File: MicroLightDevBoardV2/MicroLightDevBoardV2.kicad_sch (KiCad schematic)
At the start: 82 parts, among them J1 Conn_01x02_Socket, J10 Conn_01x02_Socket, J11 Conn_01x02_Socket, J12 TYPE-C-31-M-12, J13 Conn_01x02_Socket, J14 Conn_01x02_Socket, J15 Conn_01x02_Socket, J16 Conn_01x04_Socket, J17 Conn_01x02_Socket, J18 Conn_01x02_Socket, J19 Conn_01x04_Socket, J2 Conn_01x02_Socket, J20 Conn_01x04_Socket, J21 Conn_01x02_Socket, J22 Conn_01x02_Socket, J23 Conn_01x02_Socket, J24 Conn_01x02_Socket, J25 Conn_01x02_Socket, J26 Conn_01x04_Socket, J27 Conn_01x02_Socket, J28 Conn_01x04_Socket, J29 Conn_01x04_Socket, J3 Conn_01x04_Socket, J30 Conn_01x04_Socket, J31 Conn_01x04_Socket, J32 Conn_01x04_Socket, J33 Conn_01x04_Socket, J34 Conn_01x04_Socket, J35 Conn_01x04_Socket, J36 Conn_01x04_Socket, J37 Conn_01x04_Socket, J38 Conn_01x04_Socket, J39 Conn_01x04_Socket, J4 Conn_01x04_Socket, J40 Conn_01x04_Socket, J41 Conn_01x04_Socket, J42 Conn_01x04_Socket, J43 Conn_01x04_Socket, J44 Conn_01x04_Socket, J45 Conn_01x04_Socket, J46 Conn_01x04_Socket, J47 Conn_01x04_Socket, J48 Conn_01x04_Socket, J49 Conn_01x04_Socket, J5 Conn_01x05_Socket, J50 Conn_01x04_Socket, J6 Conn_01x05_Socket, J7 Conn_01x05_Socket, J8 Conn_01x05_Socket, J9 Conn_01x02_Socket, U1 BQ25180, U2 ATtiny3226-M, U3 S-85S1AB33-I6T1U, U4 B3U-1000P, U5 B3U-1000P, U6 USBLC6-2P6, U7 MC3479

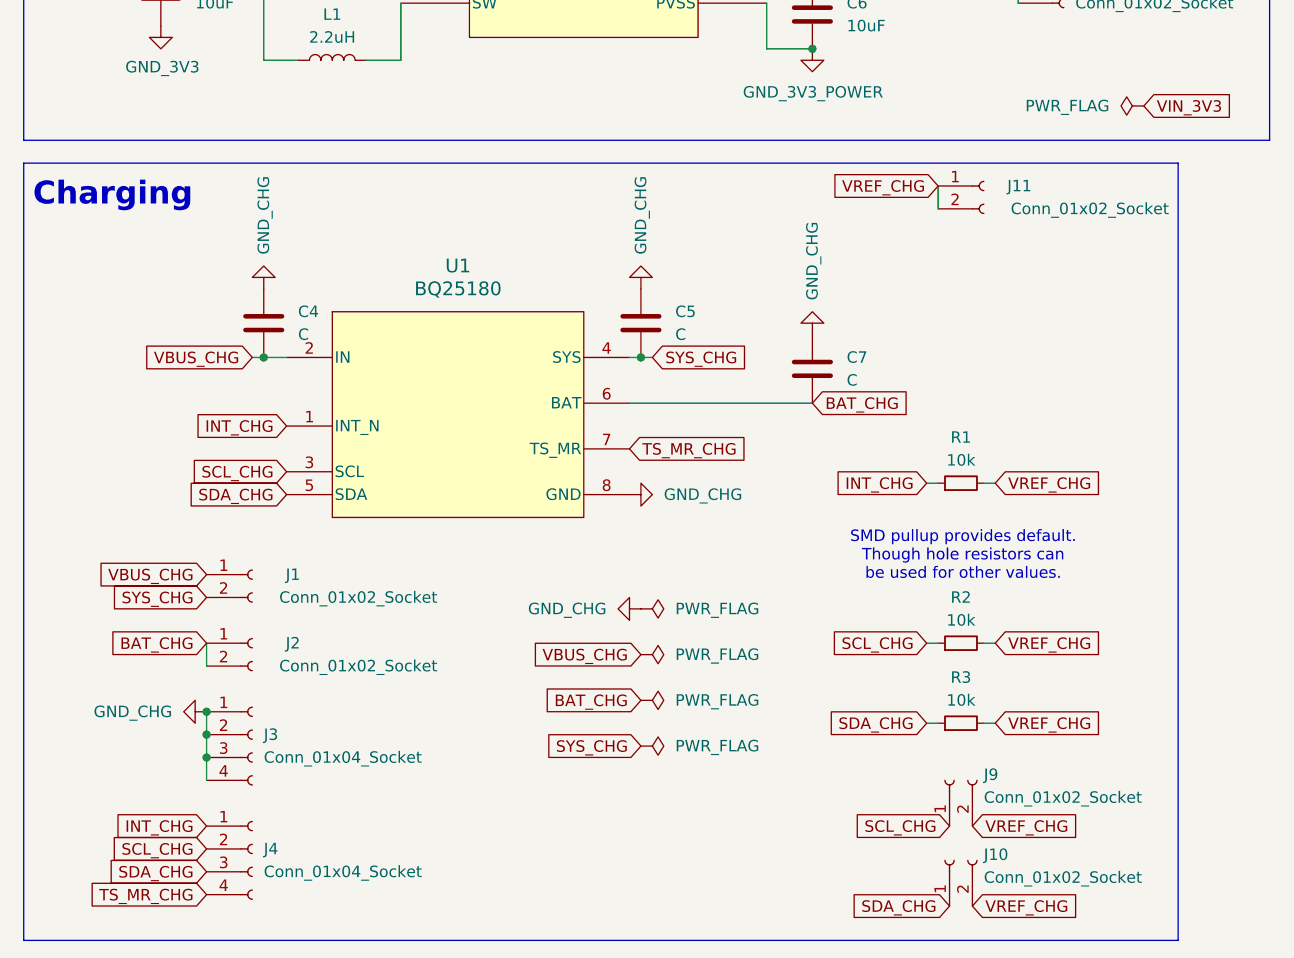
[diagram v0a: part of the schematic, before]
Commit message: added missing capacitorson charging ic pcb
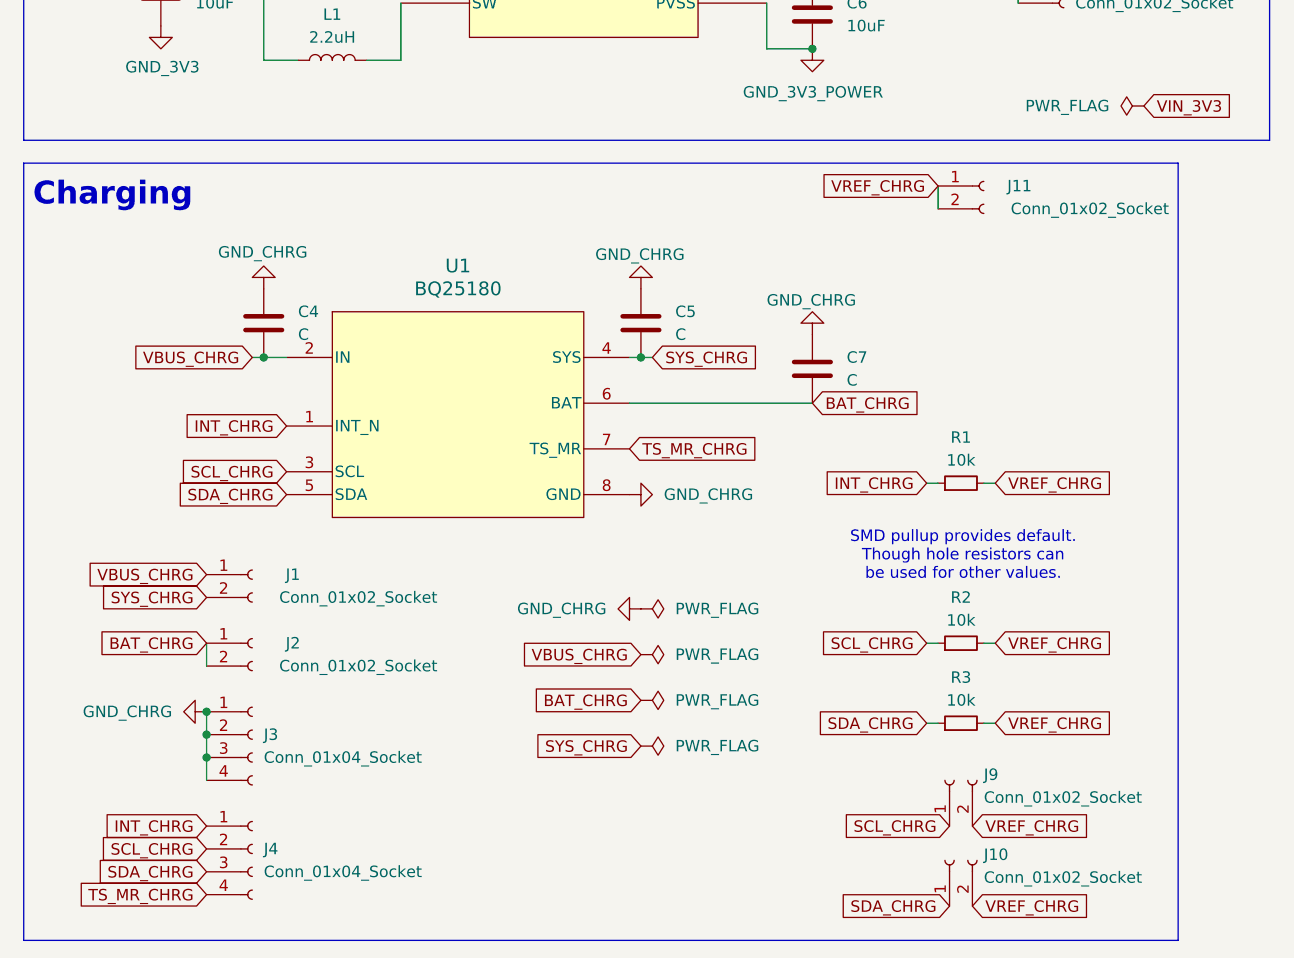
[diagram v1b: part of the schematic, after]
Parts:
- C4, C5, C7: footprint (none) -> Capacitor_SMD:C_0603_1608Metric
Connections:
- net BAT_CHG renamed BAT_CHRG
- net GND_CHG renamed GND_CHRG
- net INT_CHG renamed INT_CHRG
- net SCL_CHG renamed SCL_CHRG
- net SDA_CHG renamed SDA_CHRG
- net SYS_CHG renamed SYS_CHRG
- net TS_MR_CHG renamed TS_MR_CHRG
- net VBUS_CHG renamed VBUS_CHRG
- net VREF_CHG renamed VREF_CHRG
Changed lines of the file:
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@@
 		)
 	)
-	(global_label "VREF_CHG"
+	(global_label "VREF_CHRG"
 		(shape input)
 		(at 116.84 194.31 180)
@@
 		)
 		(property "Intersheetrefs" "${INTERSHEET_REFS}"
-			(at 104.4205 194.31 0)
+			(at 103.1505 194.31 0)
 			(effects
 				(font
@@
 		)
 	)
-	(global_label "TS_MR_CHG"
+	(global_label "TS_MR_CHRG"
 		(shape input)
 		(at 35.56 273.05 180)
@@
 		)
 		(property "Intersheetrefs" "${INTERSHEET_REFS}"
-			(at 21.8706 273.05 0)
+			(at 20.6006 273.05 0)
 			(effects
 				(font
@@
 		)
 	)
-	(global_label "BAT_CHG"
+	(global_label "BAT_CHRG"
 		(shape input)
 		(at 102.87 218.44 0)
@@
 		)
 		(property "Intersheetrefs" "${INTERSHEET_REFS}"
-			(at 114.0195 218.44 0)
+			(at 115.2895 218.44 0)
 			(effects
 				(font
@@
 		)
 	)
-	(global_label "VBUS_CHG"
+	(global_label "VBUS_CHRG"
 		(shape input)
 		(at 40.64 213.36 180)
@@
 		)
 		(property "Intersheetrefs" "${INTERSHEET_REFS}"
-			(at 27.9181 213.36 0)
+			(at 26.6481 213.36 0)
 			(effects
 				(font
@@
 		)
 	)
-	(global_label "BAT_CHG"
+	(global_label "BAT_CHRG"
 		(shape input)
 		(at 35.56 245.11 180)
@@
 		)
 		(property "Intersheetrefs" "${INTERSHEET_REFS}"
-			(at 24.4105 245.11 0)
+			(at 23.1405 245.11 0)
 			(effects
 				(font
@@
 		)
 	)
-	(global_label "VREF_CHG"
+	(global_label "VREF_CHRG"
 		(shape input)
 		(at 120.65 265.43 0)
@@
 		)
 		(property "Intersheetrefs" "${INTERSHEET_REFS}"
-			(at 133.0695 265.43 0)
+			(at 134.3395 265.43 0)
 			(effects
 				(font
@@
 		)
 	)
-	(global_label "SDA_CHG"
+	(global_label "SDA_CHRG"
 		(shape input)
 		(at 35.56 270.51 180)
@@
 		)
 		(property "Intersheetrefs" "${INTERSHEET_REFS}"
-			(at 24.1686 270.51 0)
+			(at 22.8986 270.51 0)
 			(effects
 				(font
@@
 		)
 	)
-	(global_label "SDA_CHG"
+	(global_label "SDA_CHRG"
 		(shape input)
 		(at 115.57 254 180)
@@
 		)
 		(property "Intersheetrefs" "${INTERSHEET_REFS}"
-			(at 104.1786 254 0)
+			(at 102.9086 254 0)
 			(effects
 				(font
@@
 		)
 	)
-	(global_label "VREF_CHG"
+	(global_label "VREF_CHRG"
 		(shape input)
 		(at 120.65 274.32 0)
@@
 		)
 		(property "Intersheetrefs" "${INTERSHEET_REFS}"
-			(at 133.0695 274.32 0)
+			(at 134.3395 274.32 0)
 			(effects
 				(font
@@
 		)
 	)
-	(global_label "SYS_CHG"
+	(global_label "SYS_CHRG"
 		(shape input)
 		(at 85.09 213.36 0)
@@
 		)
 		(property "Intersheetrefs" "${INTERSHEET_REFS}"
-			(at 96.4209 213.36 0)
+			(at 97.6909 213.36 0)
 			(effects
 				(font
@@
 		)
 	)
-	(global_label "SYS_CHG"
+	(global_label "SYS_CHRG"
 		(shape input)
 		(at 83.82 256.54 180)
@@
 		)
 		(property "Intersheetrefs" "${INTERSHEET_REFS}"
-			(at 72.4891 256.54 0)
+			(at 71.2191 256.54 0)
 			(effects
 				(font
@@
 		)
 	)
-	(global_label "VREF_CHG"
+	(global_label "VREF_CHRG"
 		(shape input)
 		(at 123.19 245.11 0)
@@
 		)
 		(property "Intersheetrefs" "${INTERSHEET_REFS}"
-			(at 135.6095 245.11 0)
+			(at 136.8795 245.11 0)
 			(effects
 				(font
@@
 		)
 	)
-	(global_label "TS_MR_CHG"
+	(global_label "TS_MR_CHRG"
 		(shape input)
 		(at 82.55 223.52 0)
@@
 		)
 		(property "Intersheetrefs" "${INTERSHEET_REFS}"
-			(at 96.2394 223.52 0)
+			(at 97.5094 223.52 0)
 			(effects
 				(font
@@
 		)
 	)
-	(global_label "SCL_CHG"
+	(global_label "SCL_CHRG"
 		(shape input)
 		(at 44.45 226.06 180)
@@
 		)
 		(property "Intersheetrefs" "${INTERSHEET_REFS}"
-			(at 33.1191 226.06 0)
+			(at 31.8491 226.06 0)
 			(effects
 				(font
@@
 		)
 	)
-	(global_label "VREF_CHG"
+	(global_label "VREF_CHRG"
 		(shape input)
 		(at 123.19 254 0)
@@
 		)
 		(property "Intersheetrefs" "${INTERSHEET_REFS}"
-			(at 135.6095 254 0)
+			(at 136.8795 254 0)
 			(effects
 				(font
@@
 		)
 	)
-	(global_label "SDA_CHG"
+	(global_label "SDA_CHRG"
 		(shape input)
 		(at 44.45 228.6 180)
@@
 		)
 		(property "Intersheetrefs" "${INTERSHEET_REFS}"
-			(at 33.0586 228.6 0)
+			(at 31.7886 228.6 0)
 			(effects
 				(font
@@
 		)
 	)
-	(global_label "SYS_CHG"
+	(global_label "SYS_CHRG"
 		(shape input)
 		(at 35.56 240.03 180)
@@
 		)
 		(property "Intersheetrefs" "${INTERSHEET_REFS}"
-			(at 24.2291 240.03 0)
+			(at 22.9591 240.03 0)
 			(effects
 				(font
@@
 		)
 	)
-	(global_label "VBUS_CHG"
+	(global_label "VBUS_CHRG"
 		(shape input)
 		(at 35.56 237.49 180)
@@
 		)
 		(property "Intersheetrefs" "${INTERSHEET_REFS}"
-			(at 22.8381 237.49 0)
+			(at 21.5681 237.49 0)
 			(effects
 				(font
@@
 		)
 	)
-	(global_label "INT_CHG"
+	(global_label "INT_CHRG"
 		(shape input)
 		(at 35.56 265.43 180)
@@
 		)
 		(property "Intersheetrefs" "${INTERSHEET_REFS}"
-			(at 24.8338 265.43 0)
+			(at 23.5638 265.43 0)
 			(effects
 				(font
@@
 		)
 	)
-	(global_label "VREF_CHG"
+	(global_label "VREF_CHRG"
 		(shape input)
 		(at 123.19 227.33 0)
@@
 		)
 		(property "Intersheetrefs" "${INTERSHEET_REFS}"
-			(at 135.6095 227.33 0)
+			(at 136.8795 227.33 0)
 			(effects
 				(font
@@
 		)
 	)
-	(global_label "SCL_CHG"
+	(global_label "SCL_CHRG"
 		(shape input)
 		(at 115.57 245.11 180)
@@
 		)
 		(property "Intersheetrefs" "${INTERSHEET_REFS}"
-			(at 104.2391 245.11 0)
+			(at 102.9691 245.11 0)
 			(effects
 				(font
@@
 		)
 	)
-	(global_label "SCL_CHG"
+	(global_label "SCL_CHRG"
 		(shape input)
 		(at 35.56 267.97 180)
@@
 		)
 		(property "Intersheetrefs" "${INTERSHEET_REFS}"
-			(at 24.2291 267.97 0)
+			(at 22.9591 267.97 0)
 			(effects
 				(font
@@
 		)
 	)
-	(global_label "INT_CHG"
+	(global_label "INT_CHRG"
 		(shape input)
 		(at 115.57 227.33 180)
@@
 		)
 		(property "Intersheetrefs" "${INTERSHEET_REFS}"
-			(at 104.8438 227.33 0)
+			(at 103.5738 227.33 0)
 			(effects
 				(font
@@
 		)
 	)
-	(global_label "BAT_CHG"
+	(global_label "BAT_CHRG"
 		(shape input)
 		(at 83.82 251.46 180)
@@
 		)
 		(property "Intersheetrefs" "${INTERSHEET_REFS}"
-			(at 72.6705 251.46 0)
+			(at 71.4005 251.46 0)
 			(effects
 				(font
@@
 		)
 	)
-	(global_label "SCL_CHG"
+	(global_label "SCL_CHRG"
 		(shape input)
 		(at 118.11 265.43 180)
@@
 		)
 		(property "Intersheetrefs" "${INTERSHEET_REFS}"
-			(at 106.7791 265.43 0)
+			(at 105.5091 265.43 0)
 			(effects
 				(font
@@
 		)
 	)
-	(global_label "INT_CHG"
+	(global_label "INT_CHRG"
 		(shape input)
 		(at 44.45 220.98 180)
@@
 		)
 		(property "Intersheetrefs" "${INTERSHEET_REFS}"
-			(at 33.7238 220.98 0)
+			(at 32.4538 220.98 0)
 			(effects
 				(font
@@
 		)
 	)
-	(global_label "VBUS_CHG"
+	(global_label "VBUS_CHRG"
 		(shape input)
 		(at 83.82 246.38 180)
@@
 		)
 		(property "Intersheetrefs" "${INTERSHEET_REFS}"
-			(at 71.0981 246.38 0)
+			(at 69.8281 246.38 0)
 			(effects
 				(font
@@
 		)
 	)
-	(global_label "SDA_CHG"
+	(global_label "SDA_CHRG"
 		(shape input)
 		(at 118.11 274.32 180)
@@
 		)
 		(property "Intersheetrefs" "${INTERSHEET_REFS}"
-			(at 106.7186 274.32 0)
+			(at 105.4486 274.32 0)
 			(effects
 				(font
@@
 			)
 		)
-		(property "Footprint" ""
+		(property "Footprint" "Capacitor_SMD:C_0603_1608Metric"
 			(at 42.8752 213.36 0)
 			(effects
@@
 			)
 		)
-		(property "Footprint" ""
+		(property "Footprint" "Capacitor_SMD:C_0603_1608Metric"
 			(at 84.7852 213.36 0)
 			(effects
@@
 			)
 		)
-		(property "Value" "GND_CHG"
-			(at 102.8701 207.01 90)
+		(property "Value" "GND_CHRG"
+			(at 97.79 207.01 0)
 			(effects
 				(font
@@
 			)
 		)
-		(property "Value" "GND_CHG"
+		(property "Value" "GND_CHRG"
 			(at 86.36 228.6001 90)
 			(effects
@@
 			)
 		)
-		(property "Value" "GND_CHG"
-			(at 83.8201 201.93 90)
+		(property "Value" "GND_CHRG"
+			(at 78.74 201.93 0)
 			(effects
 				(font
@@
 			)
 		)
-		(property "Footprint" ""
+		(property "Footprint" "Capacitor_SMD:C_0603_1608Metric"
 			(at 103.8352 218.44 0)
 			(effects
@@
 			)
 		)
-		(property "Value" "GND_CHG"
+		(property "Value" "GND_CHRG"
 			(at 80.01 241.2999 90)
 			(effects
@@
 			)
 		)
-		(property "Value" "GND_CHG"
+		(property "Value" "GND_CHRG"
 			(at 31.75 252.7299 90)
 			(effects
@@
 			)
 		)
-		(property "Value" "GND_CHG"
-			(at 41.9101 201.93 90)
+		(property "Value" "GND_CHRG"
+			(at 36.83 201.676 0)
 			(effects
 				(font

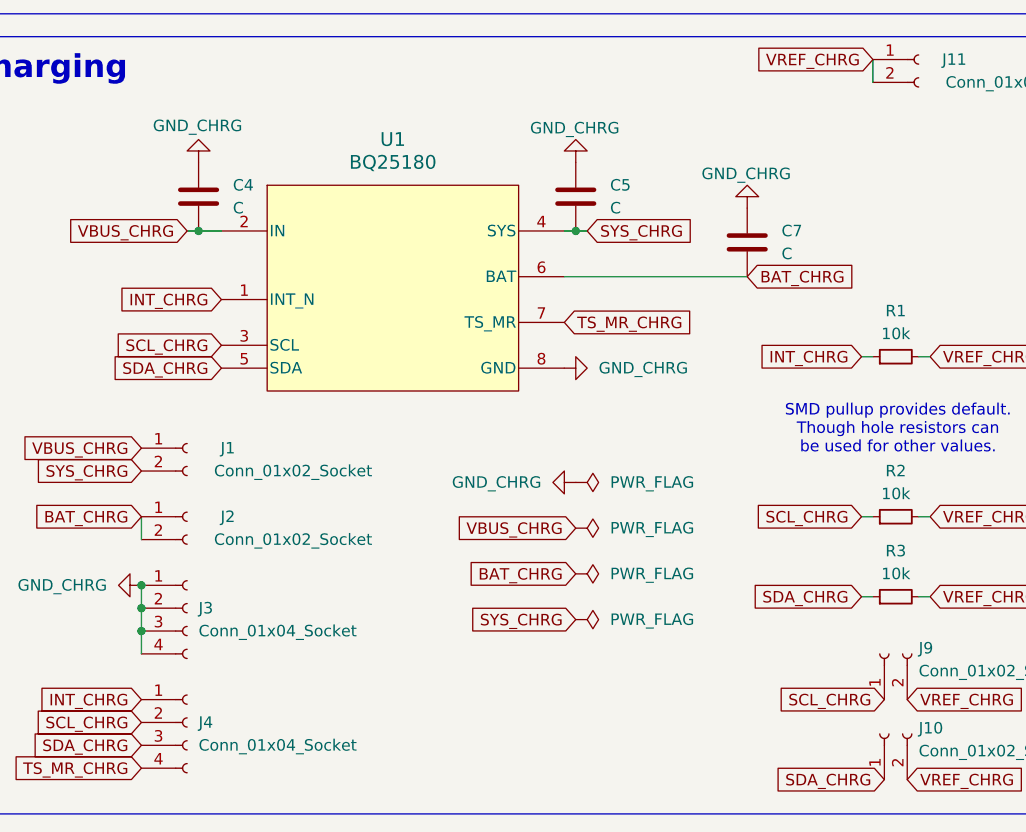
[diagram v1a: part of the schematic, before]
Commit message: added capacitor values and missing resistor on TS pin of charging ic (not using TS)
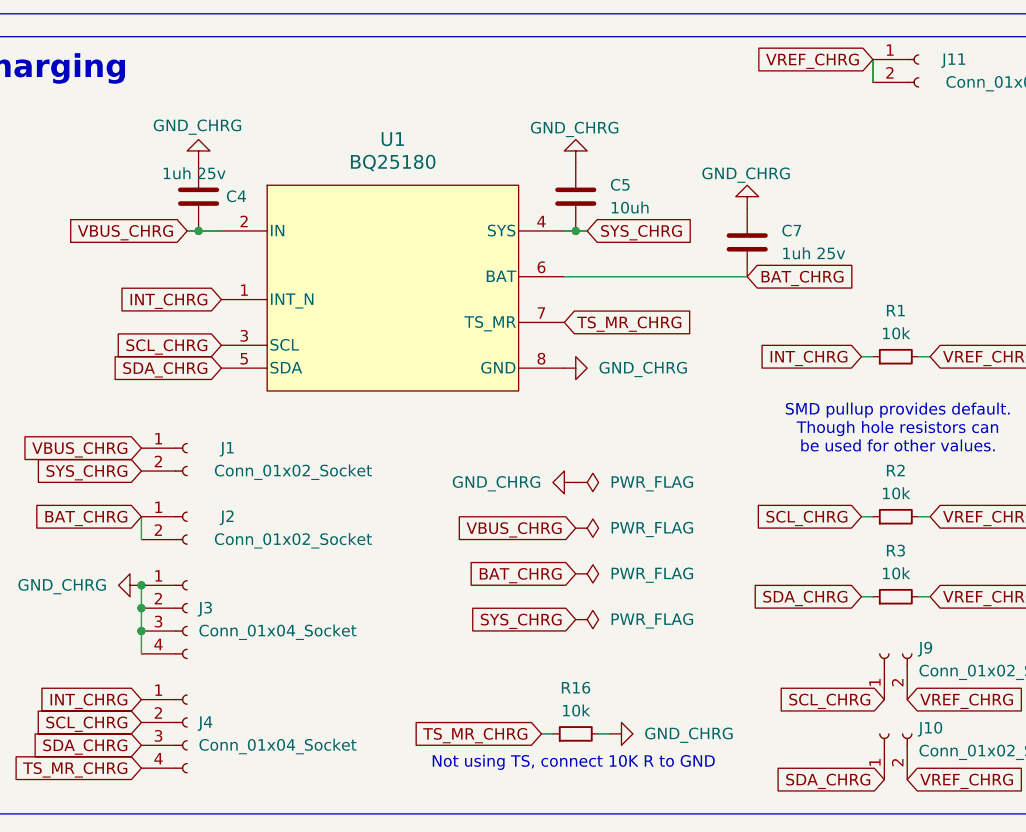
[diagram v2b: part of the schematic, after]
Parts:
- added R16: 10k, Resistor_SMD:R_0603_1608Metric, symbol Device:R_Small
- C4, C7: value C -> 1uh 25v
- C5: value C -> 10uh
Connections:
- net GND_CHRG: now also R16.2
- net TS_MR_CHRG: now also R16.1
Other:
- note added: "Not using TS, connect 10K R to GND"
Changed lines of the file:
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@@
 	(wire
 		(pts
+			(xy 86.36 269.24) (xy 87.63 269.24)
+		)
+		(stroke
+			(width 0)
+			(type default)
+		)
+	)
+	(wire
+		(pts
 			(xy 240.03 40.64) (xy 247.65 40.64)
 		)
@@
 	(wire
 		(pts
+			(xy 80.01 269.24) (xy 81.28 269.24)
+		)
+		(stroke
+			(width 0)
+			(type default)
+		)
+	)
+	(wire
+		(pts
 			(xy 121.92 245.11) (xy 123.19 245.11)
 		)
@@
 		)
 	)
+	(text "Not using TS, connect 10K R to GND"
+		(exclude_from_sim no)
+		(at 83.566 272.542 0)
+		(effects
+			(font
+				(size 1.27 1.27)
+			)
+		)
+	)
 	(text "USB / ESD"
 		(exclude_from_sim no)
@@
 		)
 	)
+	(global_label "TS_MR_CHRG"
+		(shape input)
+		(at 80.01 269.24 180)
+		(fields_autoplaced yes)
+		(effects
+			(font
+				(size 1.27 1.27)
+			)
+			(justify right)
+		)
+		(property "Intersheetrefs" "${INTERSHEET_REFS}"
+			(at 65.0506 269.24 0)
+			(effects
+				(font
+					(size 1.27 1.27)
+				)
+				(justify right)
+				(hide yes)
+			)
+		)
+	)
 	(global_label "VOUT_3V3"
 		(shape input)
@@
 		(on_board yes)
 		(dnp no)
-		(fields_autoplaced yes)
 		(property "Reference" "C4"
-			(at 45.72 208.2799 0)
+			(at 44.958 209.55 0)
 			(effects
 				(font
@@
 			)
 		)
-		(property "Value" "C"
-			(at 45.72 210.8199 0)
+		(property "Value" "1uh 25v"
+			(at 37.846 207.01 0)
 			(effects
 				(font
@@
 			)
 		)
-		(property "Value" "C"
+		(property "Value" "10uh"
 			(at 87.63 210.8199 0)
 			(effects
@@
 	(symbol
 		(lib_id "power:GND")
+		(at 87.63 269.24 90)
+		(unit 1)
+		(exclude_from_sim no)
+		(in_bom yes)
+		(on_board yes)
+		(dnp no)
+		(property "Reference" "#PWR035"
+			(at 93.98 269.24 0)
+			(effects
+				(font
+					(size 1.27 1.27)
+				)
+				(hide yes)
+			)
+		)
+		(property "Value" "GND_CHRG"
+			(at 91.44 269.2401 90)
+			(effects
+				(font
+					(size 1.27 1.27)
+				)
+				(justify right)
+			)
+		)
+		(property "Footprint" ""
+			(at 87.63 269.24 0)
+			(effects
+				(font
+					(size 1.27 1.27)
+				)
+				(hide yes)
+			)
+		)
+		(property "Datasheet" ""
+			(at 87.63 269.24 0)
+			(effects
+				(font
+					(size 1.27 1.27)
+				)
+				(hide yes)
+			)
+		)
+		(property "Description" "Power symbol creates a global label with name \"GND\" , ground"
+			(at 87.63 269.24 0)
+			(effects
+				(font
+					(size 1.27 1.27)
+				)
+				(hide yes)
+			)
+		)
+		(pin "1"
+		)
+		(instances
+			(project "MicroLightDevBoardV2"
+				(path "/4d4b60a6-56d4-4632-90b9-cd9e4f577154"
+					(reference "#PWR035")
+					(unit 1)
+				)
+			)
+		)
+	)
+	(symbol
+		(lib_id "power:GND")
 		(at 125.73 166.37 270)
 		(unit 1)
@@
 			)
 		)
-		(property "Value" "C"
+		(property "Value" "1uh 25v"
 			(at 106.68 215.8999 0)
 			(effects
@@
 					(unit 1)
 				)
+			)
+		)
+	)
+	(symbol
+		(lib_id "Device:R_Small")
+		(at 83.82 269.24 90)
+		(unit 1)
+		(exclude_from_sim no)
+		(in_bom yes)
+		(on_board yes)
+		(dnp no)
+		(fields_autoplaced yes)
+		(property "Reference" "R16"
+			(at 83.82 264.16 90)
+			(effects
+				(font
+					(size 1.27 1.27)
+				)
+			)
+		)
+		(property "Value" "10k"
+			(at 83.82 266.7 90)
+			(effects
+				(font
+					(size 1.27 1.27)
+				)
+			)
+		)
+		(property "Footprint" "Resistor_SMD:R_0603_1608Metric"
+			(at 83.82 269.24 0)
+			(effects
+				(font
+					(size 1.27 1.27)
+				)
+				(hide yes)
+			)
+		)
+		(property "Datasheet" "~"
+			(at 83.82 269.24 0)
+			(effects
+				(font
+					(size 1.27 1.27)
+				)
+				(hide yes)
+			)
+		)
+		(property "Description" "Resistor, small symbol"
+			(at 83.82 269.24 0)
+			(effects
+				(font
+					(size 1.27 1.27)
+				)
+				(hide yes)
+			)
+		)
+		(pin "1"
+		)
+		(pin "2"
+		)
+		(instances
+			(project "MicroLightDevBoardV2"
+				(path "/4d4b60a6-56d4-4632-90b9-cd9e4f577154"
+					(reference "R16")
+					(unit 1)
+				)
